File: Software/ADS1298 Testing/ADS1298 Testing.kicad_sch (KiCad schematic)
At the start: 12 parts, among them U1 ADS1298xPAG, U3 ESP32-S3-DevKitC

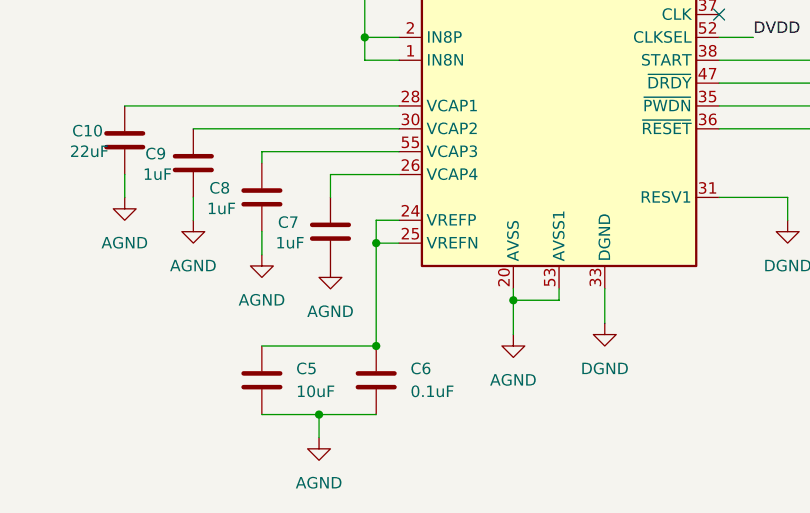
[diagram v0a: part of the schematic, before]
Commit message: Fixed VREFP /VREFN connection for using internal 2.4V reference
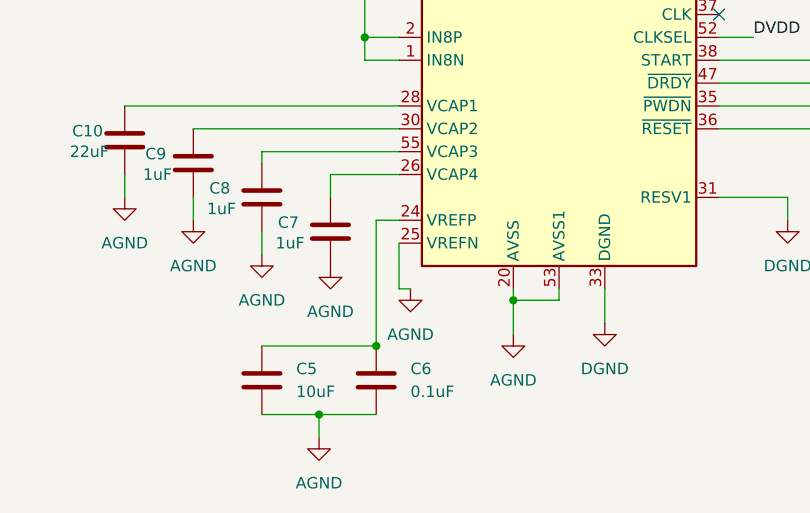
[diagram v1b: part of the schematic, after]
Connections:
- net AGND: now also U1.25 (VREFN)
- net at C5.1, C6.1, U1.24 (VREFP): no longer U1.25 (VREFN)
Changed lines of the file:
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@@
-	)
-	(junction
-		(at 83.82 114.3)
-		(diameter 0)
-		(color 0 0 0 0)
 	)
 	(junction
@@
 		)
 	)
+	(wire
+		(pts
+			(xy 86.36 119.38) (xy 86.36 114.3)
+		)
+		(stroke
+			(width 0)
+			(type default)
+		)
+	)
 	(polyline
 		(pts
@@
 	(wire
 		(pts
-			(xy 83.82 114.3) (xy 86.36 114.3)
-		)
-		(stroke
-			(width 0)
-			(type default)
-		)
-	)
-	(wire
-		(pts
 			(xy 82.55 50.8) (xy 82.55 48.26)
 		)
@@
 	(wire
 		(pts
+			(xy 87.63 119.38) (xy 86.36 119.38)
+		)
+		(stroke
+			(width 0)
+			(type default)
+		)
+	)
+	(wire
+		(pts
 			(xy 236.22 71.12) (xy 243.84 71.12)
 		)
@@
 		)
 	)
-	(wire
-		(pts
-			(xy 83.82 111.76) (xy 83.82 114.3)
-		)
-		(stroke
-			(width 0)
-			(type default)
-		)
-	)
 	(polyline
 		(pts
@@
 	(wire
 		(pts
-			(xy 83.82 114.3) (xy 83.82 125.73)
+			(xy 83.82 111.76) (xy 83.82 125.73)
 		)
 		(stroke
@@
 					(unit 1)
 				)
+			)
+		)
+	)
+	(symbol
+		(lib_id "power:GND")
+		(at 87.63 119.38 0)
+		(unit 1)
+		(exclude_from_sim no)
+		(in_bom yes)
+		(on_board yes)
+		(dnp no)
+		(fields_autoplaced yes)
+		(property "Reference" "#PWR020"
+			(at 87.63 125.73 0)
+			(effects
+				(font
+					(size 1.27 1.27)
+				)
+				(hide yes)
+			)
+		)
+		(property "Value" "AGND"
+			(at 87.63 124.46 0)
+			(effects
+				(font
+					(size 1.27 1.27)
+				)
+			)
+		)
+		(property "Footprint" ""
+			(at 87.63 119.38 0)
+			(effects
+				(font
+					(size 1.27 1.27)
+				)
+				(hide yes)
+			)
+		)
+		(property "Datasheet" ""
+			(at 87.63 119.38 0)
+			(effects
+				(font
+					(size 1.27 1.27)
+				)
+				(hide yes)
+			)
+		)
+		(property "Description" "Power symbol creates a global label with name \"GND\" , ground"
+			(at 87.63 119.38 0)
+			(effects
+				(font
+					(size 1.27 1.27)
+				)
+				(hide yes)
+			)
+		)
+		(pin "1"
+		)
+		(instances
+			(project "ADS1298 Testing"
+				(path "/f2e31a23-3ecd-40a1-a4c2-8d65099396ff"
+					(reference "#PWR020")
+					(unit 1)
+				)
